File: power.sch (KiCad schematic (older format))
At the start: 37 parts, among them Q1 DMP6050SFG, U1 LT8609, U2 LT8609

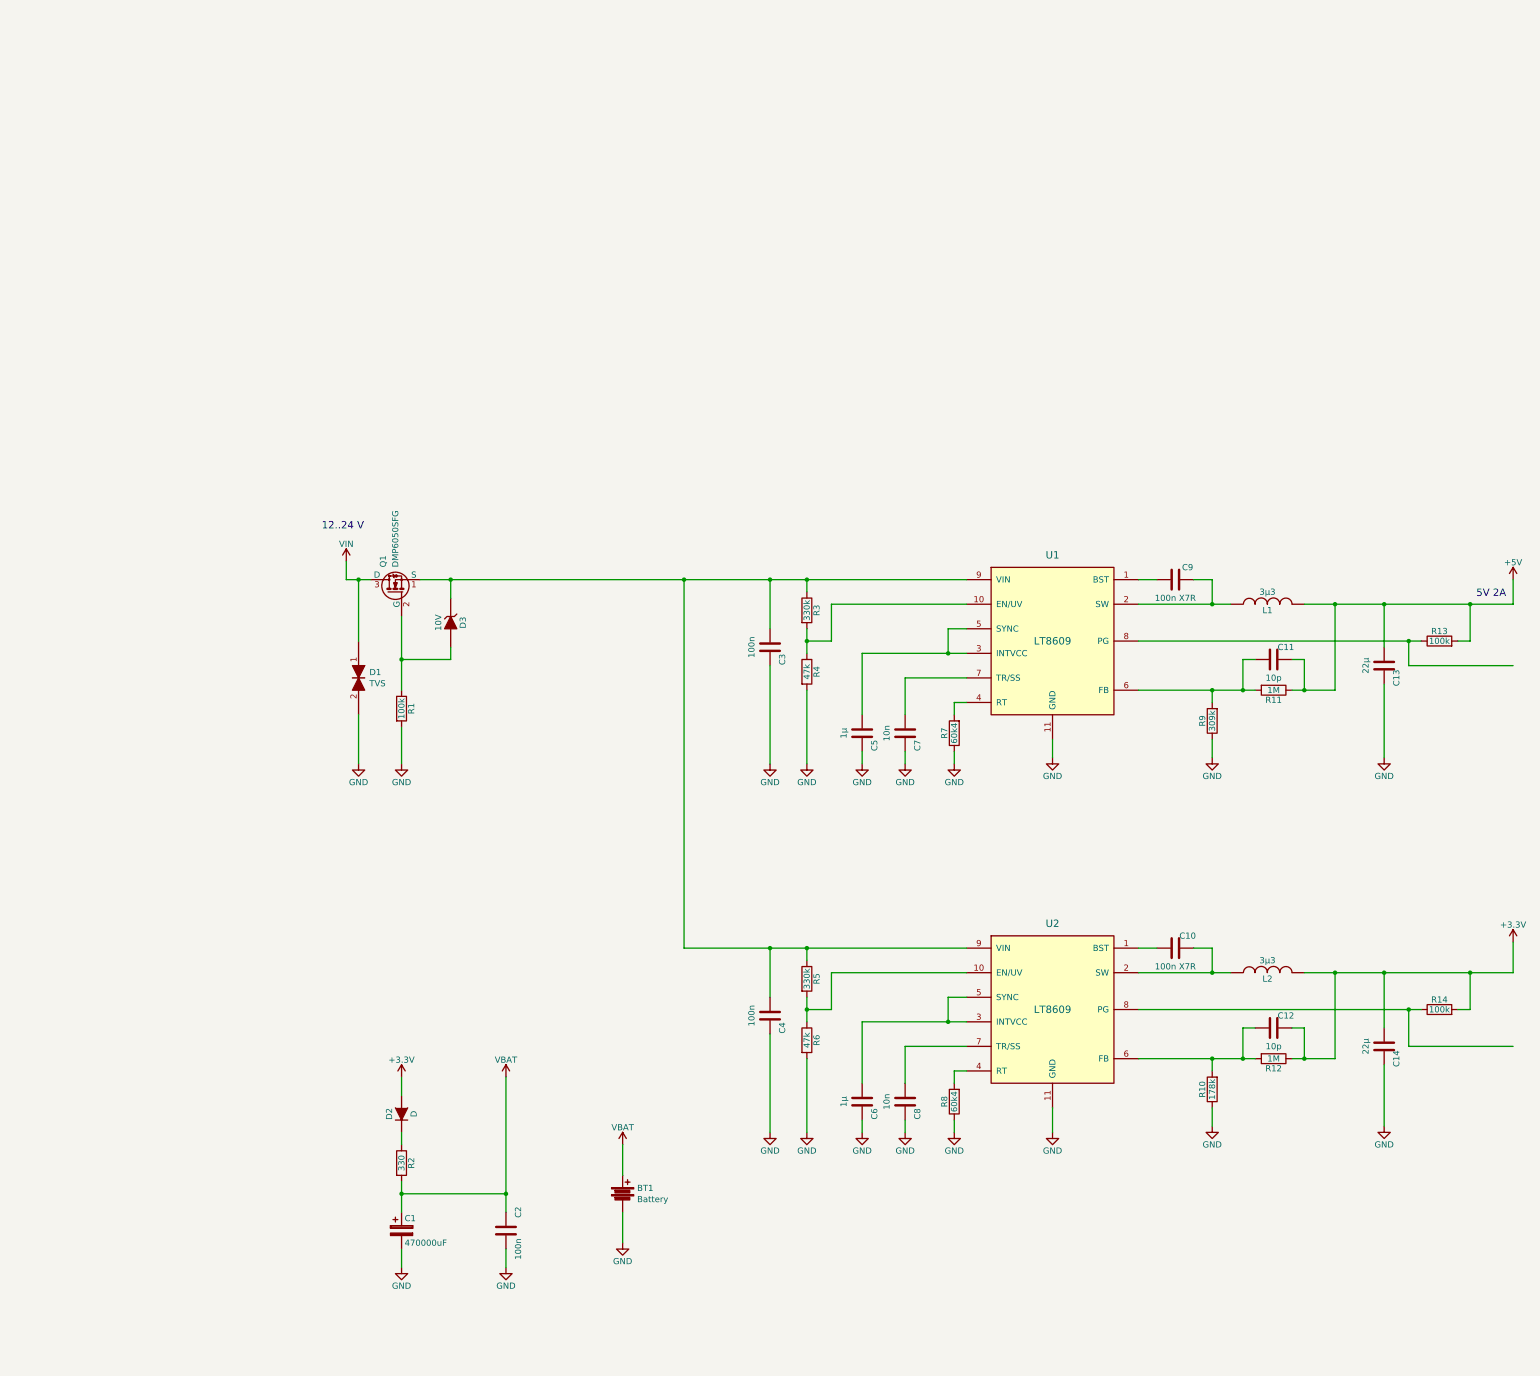
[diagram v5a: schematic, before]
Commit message: Use TPS5401 converter
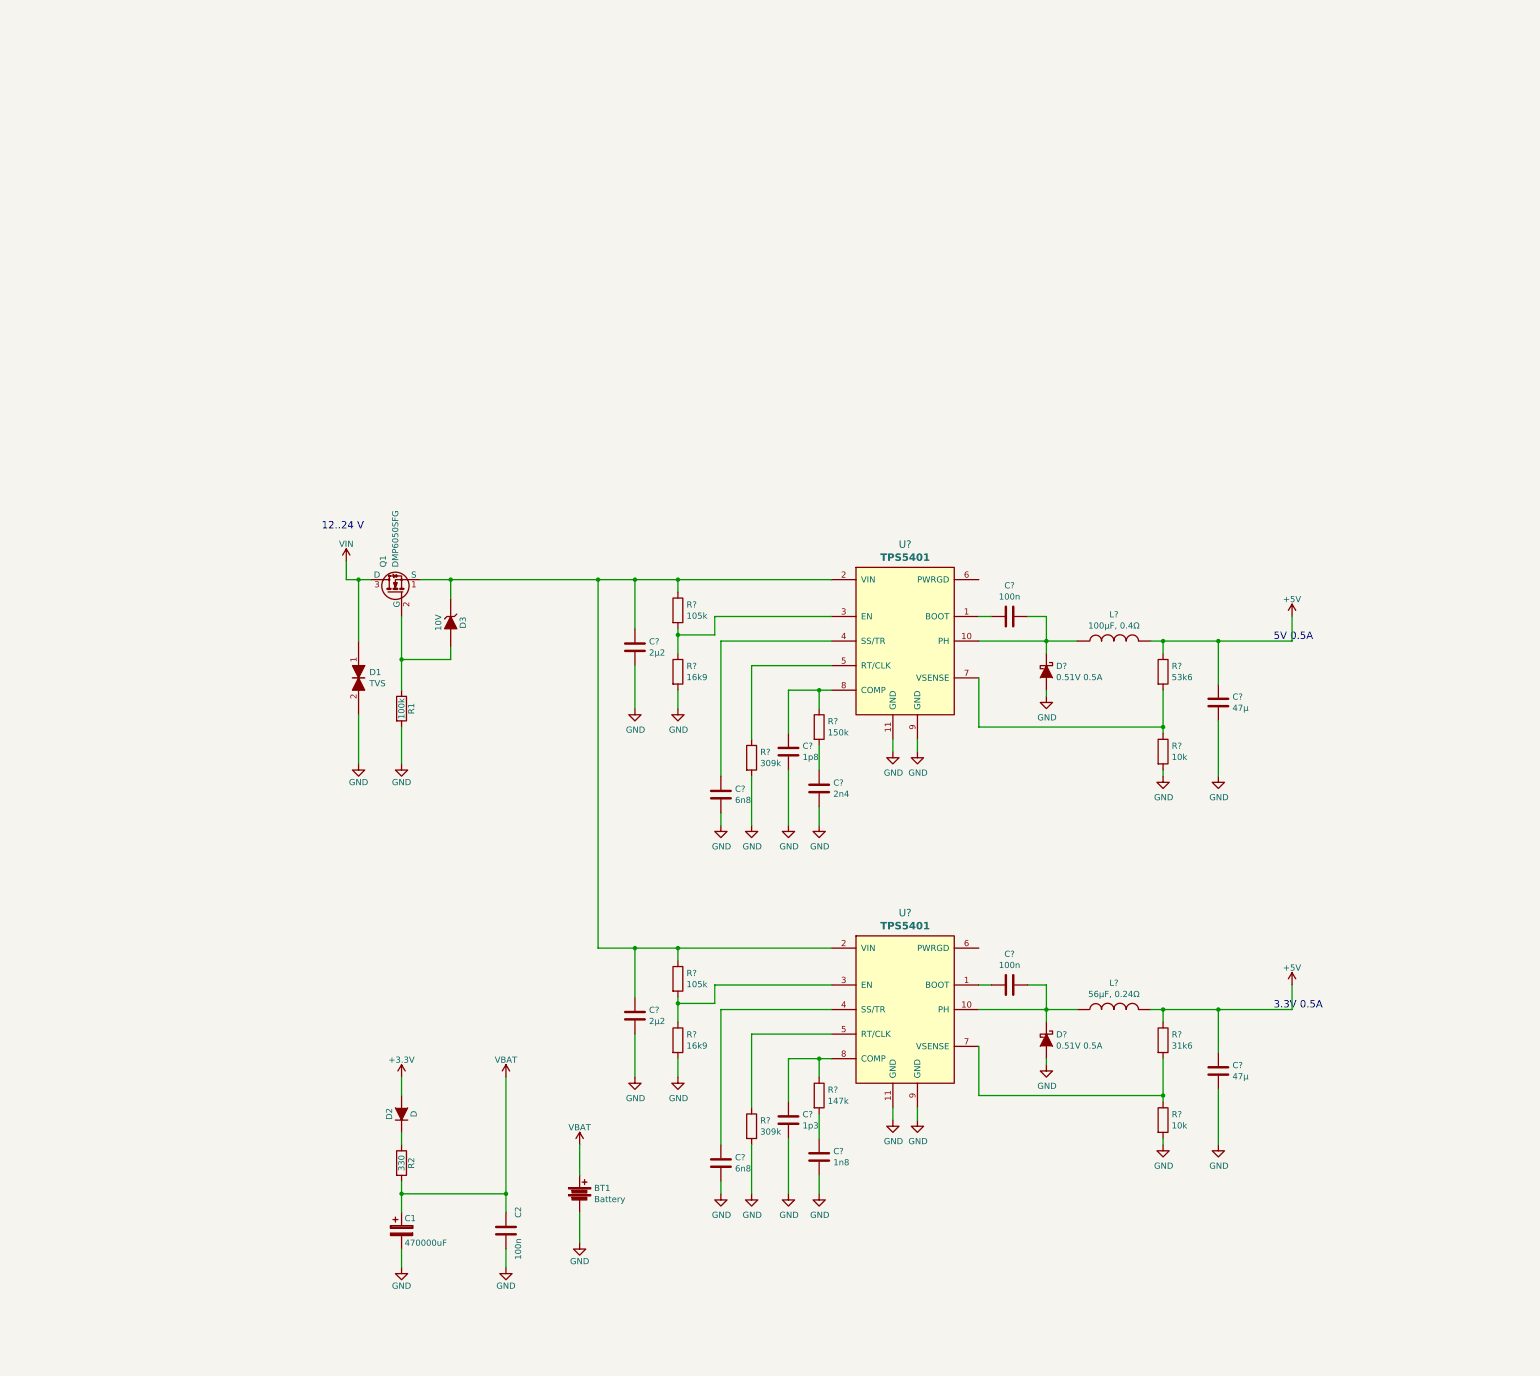
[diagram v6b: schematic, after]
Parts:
- removed C10, C9: 100n X7R, Capacitors_SMD:C_0603_HandSoldering, symbol C
- removed C11, C12: 10p, Capacitors_SMD:C_0603_HandSoldering, symbol C
- removed C13, C14: 22µ, symbol C
- removed C3, C4: 100n, Capacitors_SMD:C_0603_HandSoldering, symbol C
- removed C5, C6: 1µ, Capacitors_SMD:C_0603_HandSoldering, symbol C
- removed C7, C8: 10n, Capacitors_SMD:C_0603_HandSoldering, symbol C
- removed L1, L2: 3µ3, symbol INDUCTOR
- removed R10: 178k, Resistors_SMD:R_0603_HandSoldering, symbol R
- removed R11, R12: 1M, Resistors_SMD:R_0603_HandSoldering, symbol R
- removed R13, R14: 100k, Resistors_SMD:R_0603_HandSoldering, symbol R
- removed R3, R5: 330k, Resistors_SMD:R_0603_HandSoldering, symbol R
- removed R4, R6: 47k, Resistors_SMD:R_0603_HandSoldering, symbol R
- removed R7, R8: 60k4, Resistors_SMD:R_0603_HandSoldering, symbol R
- removed R9: 309k, Resistors_SMD:R_0603_HandSoldering, symbol R
- removed U1, U2: LT8609, symbol LT8609
- added C? (x2): 2µ2, symbol C
- added C?: 1p8, symbol C
- added C?: 2n4, symbol C
- added C? (x2): 6n8, symbol C
- added C? (x2): 100n, symbol C
- added C? (x2): 47µ, symbol C
- added C?: 1p3, symbol C
- added C?: 1n8, symbol C
- added D? (x2): 0.51V 0.5A, symbol D_Schottky
- added L?: 100µF, 0.4Ω, symbol INDUCTOR
- added L?: 56µF, 0.24Ω, symbol INDUCTOR
- added R? (x2): 105k, symbol R
- added R? (x2): 16k9, symbol R
- added R?: 150k, symbol R
- added R? (x2): 309k, symbol R
- added R?: 53k6, symbol R
- added R? (x2): 10k, symbol R
- added R?: 147k, symbol R
- added R?: 31k6, symbol R
- added U? (x2): TPS5401, symbol TPS5401
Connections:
- net +5V: now also C?.1, C?.1, L?.2, L?.2, R?.1, R?.1
- net GND: now also C?.2, C?.2, C?.2, C?.2, C?.2, C?.2, C?.2, C?.2, C?.2, C?.2, D?.2 (A), D?.2 (A), R?.2, R?.2, R?.2, R?.2, R?.2, R?.2, U?.11 (GND), U?.11 (GND), U?.9 (GND), U?.9 (GND)
- net at D3.1 (K), Q1.1 (S): now also C?.1, C?.1, R?.1, R?.1, U?.2 (VIN), U?.2 (VIN)
- new net: C?.2, U?.1 (BOOT) (x2)
- new net: C?.1, D?.1 (K), L?.1, U?.10 (PH) (x2)
- new net: R?.1, R?.2, U?.3 (EN) (x2)
- new net: C?.1, U?.4 (SS/TR) (x2)
- new net: R?.1, U?.5 (RT/CLK) (x2)
- new net: R?.1, R?.2, U?.7 (VSENSE) (x2)
- new net: C?.1, R?.1, U?.8 (COMP) (x2)
- new net: C?.1, R?.2 (x2)
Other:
- note added: "3.3V 0.5A"
- note added: "5V 0.5A"
- note removed: "5V 2A"
- moved on the sheet: BT1

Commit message: Use TI TCAN334 3.3V CAN transceiver.
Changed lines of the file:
@@
 	1200 5900 1200 6000
 Wire Wire Line
-	1200 6300 1200 6400
-Wire Wire Line
-	1200 6400 1200 6550
+	1200 6300 1200 6550
 Wire Wire Line
 	1200 6850 1200 7000
@@
 	1200 6400 2050 6400
 Wire Wire Line
-	2050 5450 2050 6400
-Wire Wire Line
-	2050 6400 2050 6550
+	2050 5450 2050 6550
 Connection ~ 1200 6400
 Connection ~ 2050 6400
@@
 	1600 1950 1600 2050
 Wire Wire Line
-	1200 1700 1200 2050
-Wire Wire Line
-	1200 2050 1200 2300
+	1200 1700 1200 2300
 Wire Wire Line
 	1600 2050 1200 2050
@@
 Connection ~ 1600 1400
 Wire Wire Line
-	750  1400 850  1400
-Wire Wire Line
-	850  1400 950  1400
+	750  1400 950  1400
 Wire Wire Line
 	2650 6000 2650 6250
@@
 	850  2900 850  2500
 Wire Wire Line
-	1350 1400 1600 1400
-Wire Wire Line
-	1600 1400 2800 1400
-Wire Wire Line
-	2800 1400 3100 1400
-Wire Wire Line
-	3100 1400 3450 1400
-Wire Wire Line
-	3450 1400 4700 1400
+	1350 1400 4700 1400
 Wire Wire Line
 	3450 1500 3450 1400
 Connection ~ 3450 1400
 Wire Wire Line
-	3450 1800 3450 1850
-Wire Wire Line
-	3450 1850 3450 2000
+	3450 1800 3450 2000
 Wire Wire Line
 	3450 2300 3450 2450
@@
 	4600 2750 4600 2950
 Wire Wire Line
-	4350 2300 4600 2300
-Wire Wire Line
-	4600 2300 4700 2300
+	4350 2300 4700 2300
 Wire Wire Line
 	4350 2300 4350 2650
@@
 Connection ~ 4600 2300
 Wire Wire Line
-	5900 1900 6450 1900
-Wire Wire Line
-	6450 1900 6700 1900
-Wire Wire Line
-	6450 1700 6450 1900
-Wire Wire Line
-	6450 1900 6450 2000
+	5900 1900 6700 1900
+Wire Wire Line
+	6450 1700 6450 2000
 Connection ~ 6450 1900
 Wire Wire Line
-	7300 1900 7400 1900
-Wire Wire Line
-	7400 1900 7850 1900
-Wire Wire Line
-	7850 1900 8450 1900
+	7300 1900 8450 1900
 Wire Wire Line
 	7400 2000 7400 1900
 Connection ~ 7400 1900
 Wire Wire Line
-	7400 2300 7400 2600
-Wire Wire Line
-	7400 2600 7400 2650
+	7400 2300 7400 2650
 Wire Wire Line
 	5900 2200 5900 2600
@@
 $EndComp
 Wire Wire Line
-	2800 4400 3100 4400
-Wire Wire Line
-	3100 4400 3450 4400
-Wire Wire Line
-	3450 4400 4700 4400
+	2800 4400 4700 4400
 Wire Wire Line
 	3450 4500 3450 4400
 Connection ~ 3450 4400
 Wire Wire Line
-	3450 4800 3450 4850
-Wire Wire Line
-	3450 4850 3450 5000
+	3450 4800 3450 5000
 Wire Wire Line
 	3450 5300 3450 5450
@@
 	4600 5750 4600 5950
 Wire Wire Line
-	4350 5300 4600 5300
-Wire Wire Line
-	4600 5300 4700 5300
+	4350 5300 4700 5300
 Wire Wire Line
 	4350 5300 4350 5650
@@
 Connection ~ 4600 5300
 Wire Wire Line
-	5900 4900 6450 4900
-Wire Wire Line
-	6450 4900 6700 4900
-Wire Wire Line
-	6450 4700 6450 4900
-Wire Wire Line
-	6450 4900 6450 5000
+	5900 4900 6700 4900
+Wire Wire Line
+	6450 4700 6450 5000
 Connection ~ 6450 4900
 Wire Wire Line
-	7300 4900 7400 4900
-Wire Wire Line
-	7400 4900 7850 4900
-Wire Wire Line
-	7850 4900 8450 4900
+	7300 4900 8450 4900
 Wire Wire Line
 	7400 5000 7400 4900
 Connection ~ 7400 4900
 Wire Wire Line
-	7400 5300 7400 5600
-Wire Wire Line
-	7400 5600 7400 5650
+	7400 5300 7400 5650
 Wire Wire Line
 	5900 5200 5900 5600

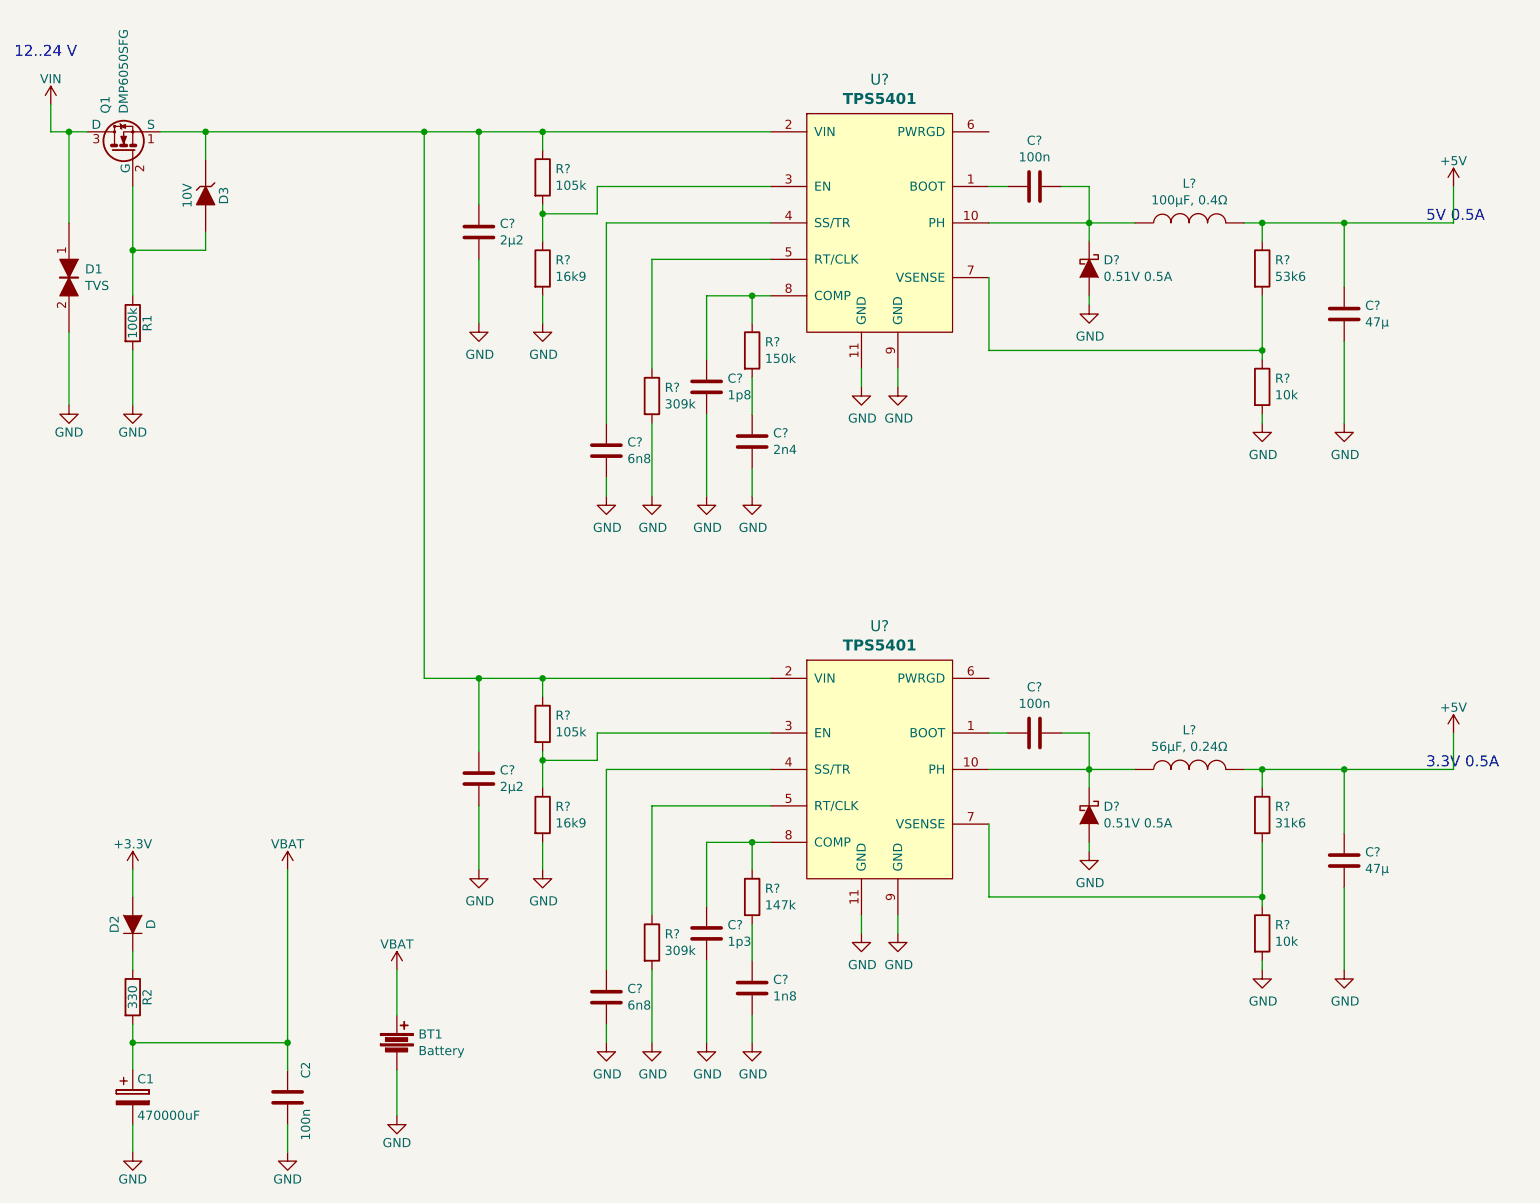
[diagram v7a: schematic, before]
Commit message: Remove 5V supply
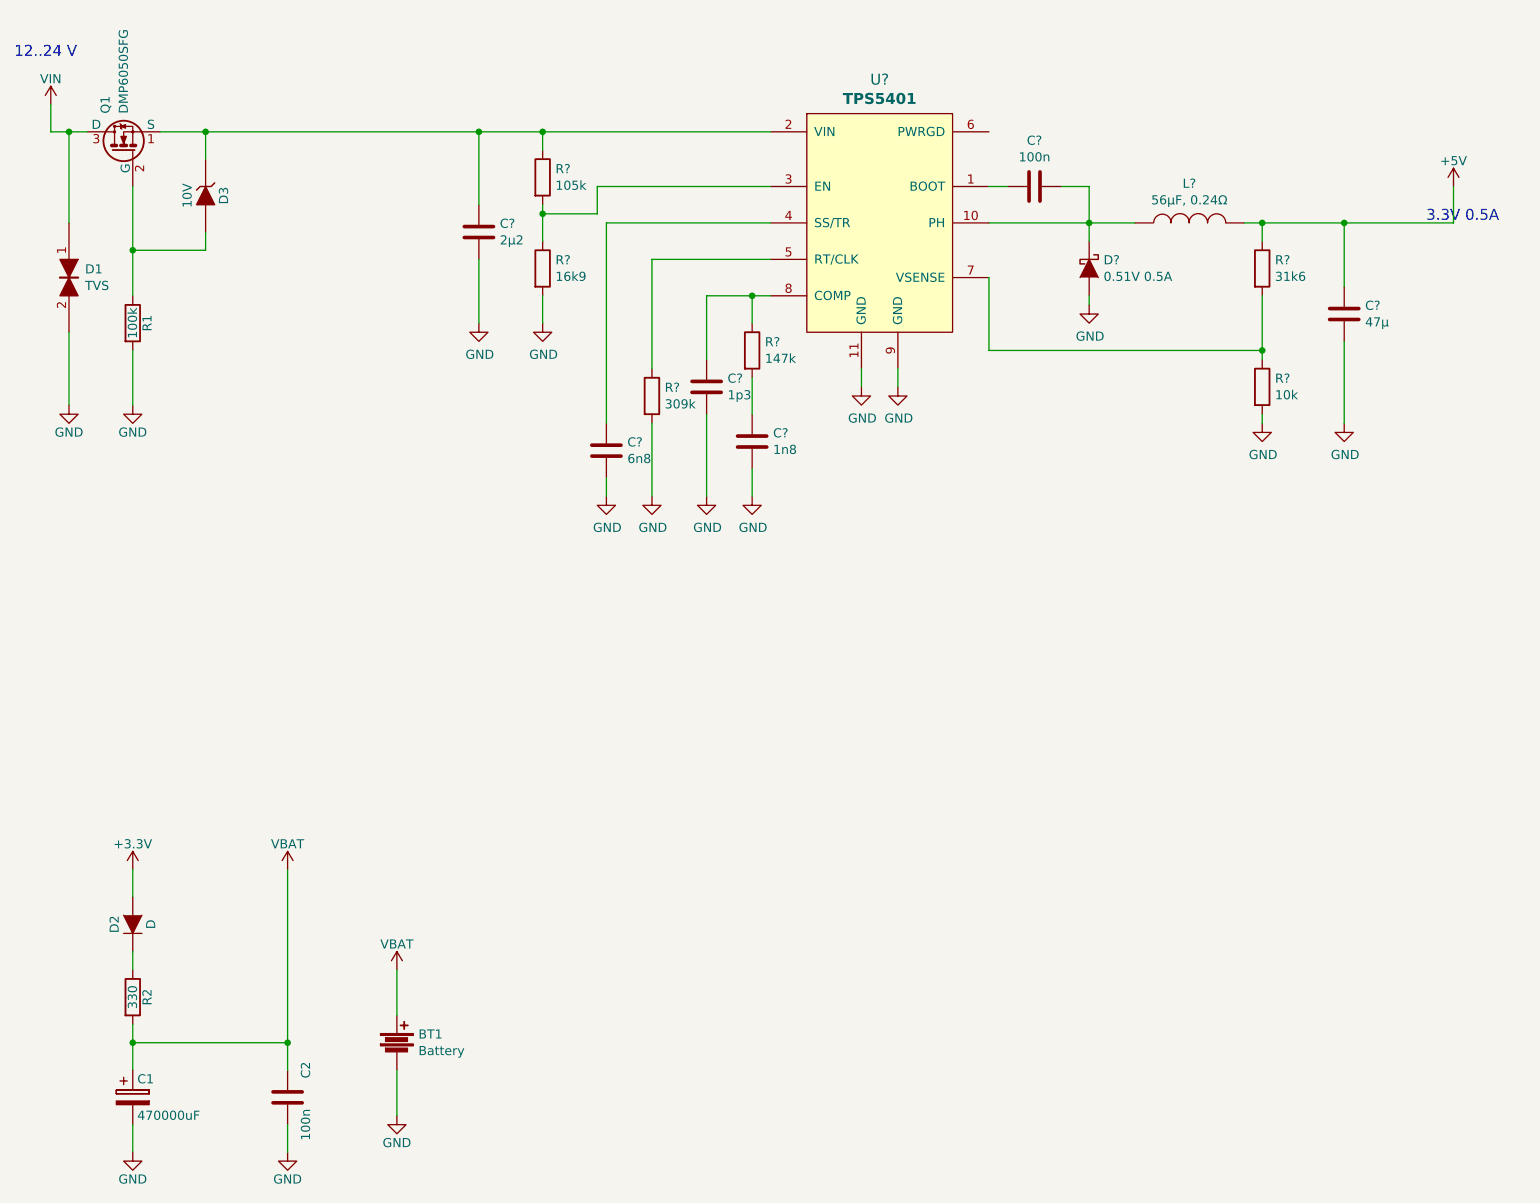
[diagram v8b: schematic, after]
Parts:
- removed C?: 2µ2, symbol C
- removed C?: 1p8, symbol C
- removed C?: 2n4, symbol C
- removed C?: 6n8, symbol C
- removed C?: 100n, symbol C
- removed C?: 47µ, symbol C
- removed D?: 0.51V 0.5A, symbol D_Schottky
- removed L?: 100µF, 0.4Ω, symbol INDUCTOR
- removed R?: 105k, symbol R
- removed R?: 16k9, symbol R
- removed R?: 150k, symbol R
- removed R?: 309k, symbol R
- removed R?: 53k6, symbol R
- removed R?: 10k, symbol R
- removed U?: TPS5401, symbol TPS5401
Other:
- note removed: "5V 0.5A"
- moved on the sheet: C?, D?, L?, R?, U?
